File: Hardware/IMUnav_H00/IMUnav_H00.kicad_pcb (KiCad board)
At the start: 4 copper layers, 219 parts, among them J1 Conn_01x03_Pin, J2 Conn_01x03_Pin, J3 Conn_01x03_Pin, J4 Conn_01x03_Pin, J5 Conn_01x03_Pin, J6 Conn_01x03_Pin, J7 918-418K2023S40001, J8 Conn_Coaxial, J9 Micro_SD_Card_Det_Hirose_DM3AT, Q1 S8050, Q2 S8050, SW1 MT-102, SW2 SW_SPST, SW3 SW_SPST, SW4 SW_SPST, SW5 SW_SPST, U1 STM32F446VETx, U10 ESP32-C3-MINI-1, U11 MPU-6050, U12 LSM303C, U13 ADIS16505-2BMLZ, U14 ADIS16505-x/PCBZ, U15 XC6206P332MR, U16 NEO-M8U, U17 XT25F256BWSIGT, U18 OLED_I2C, U2 TVS0500DRV, U3 74LVC2G02, U4 BQ24075RGT, U5 USBLC6-2P6, U6 HT7533-1, U7 TPS62823DLC, U8 USB2514B-AEZC-TR, U9 CH340G, X1 SX5M24.000M20F30TNN, X2 SX5M24.000M20F30TNN

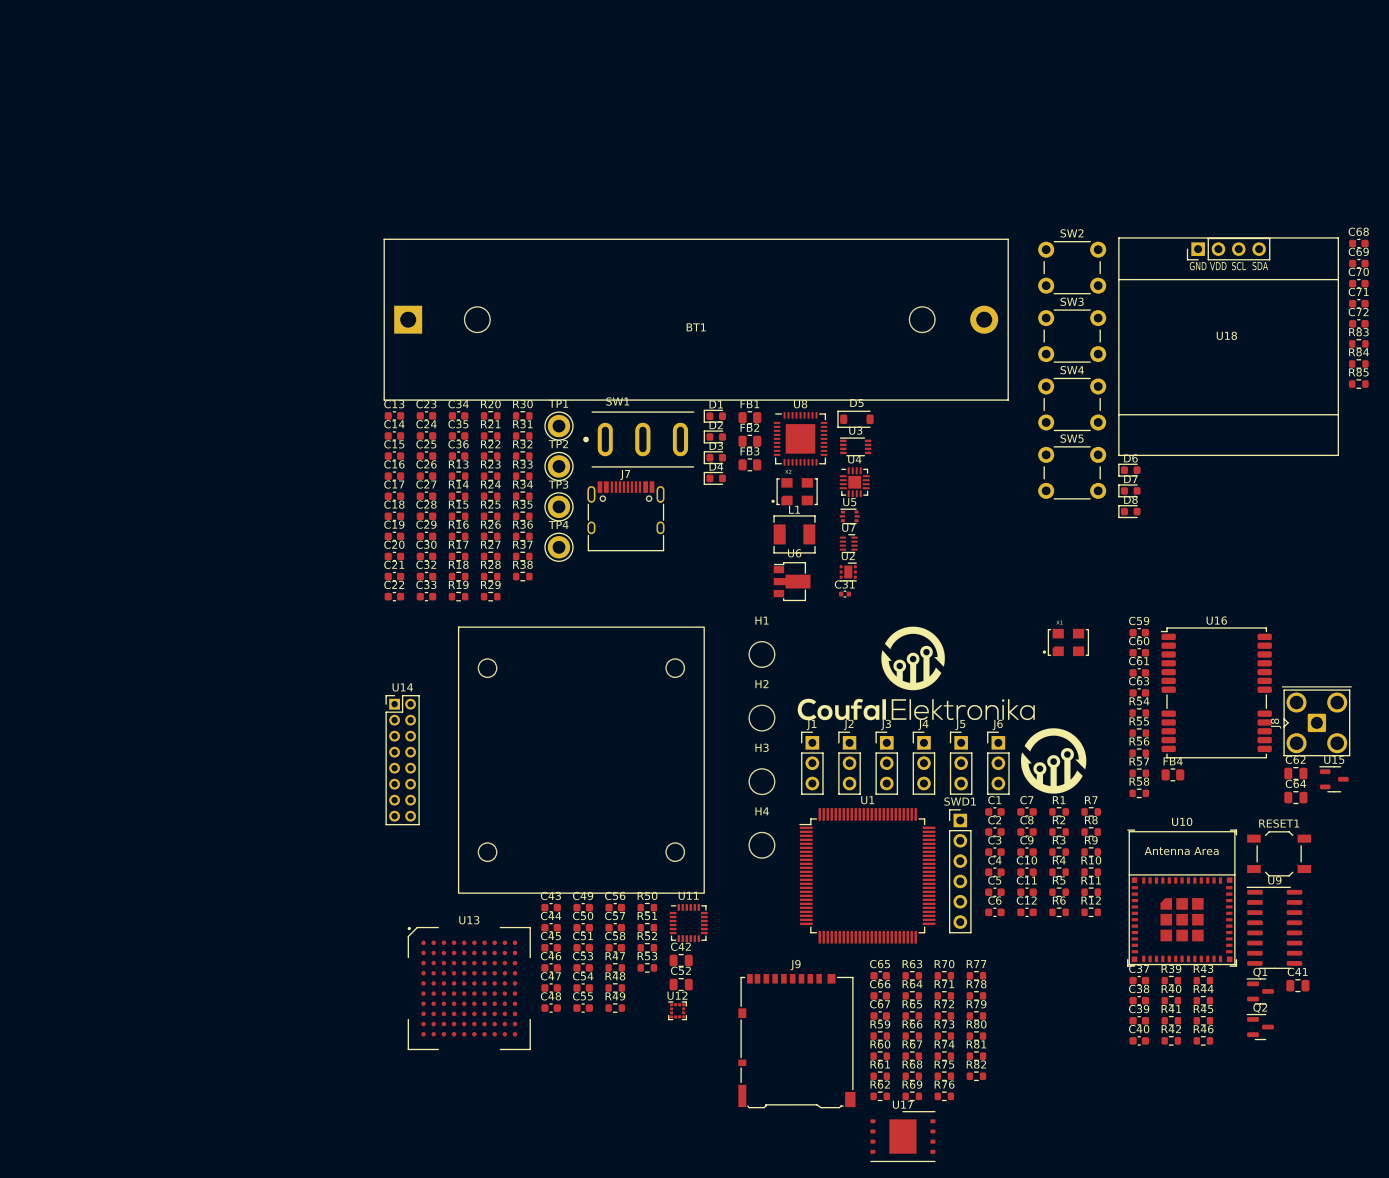
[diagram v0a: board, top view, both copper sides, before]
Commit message: Created PCB, configured stackup and DRC
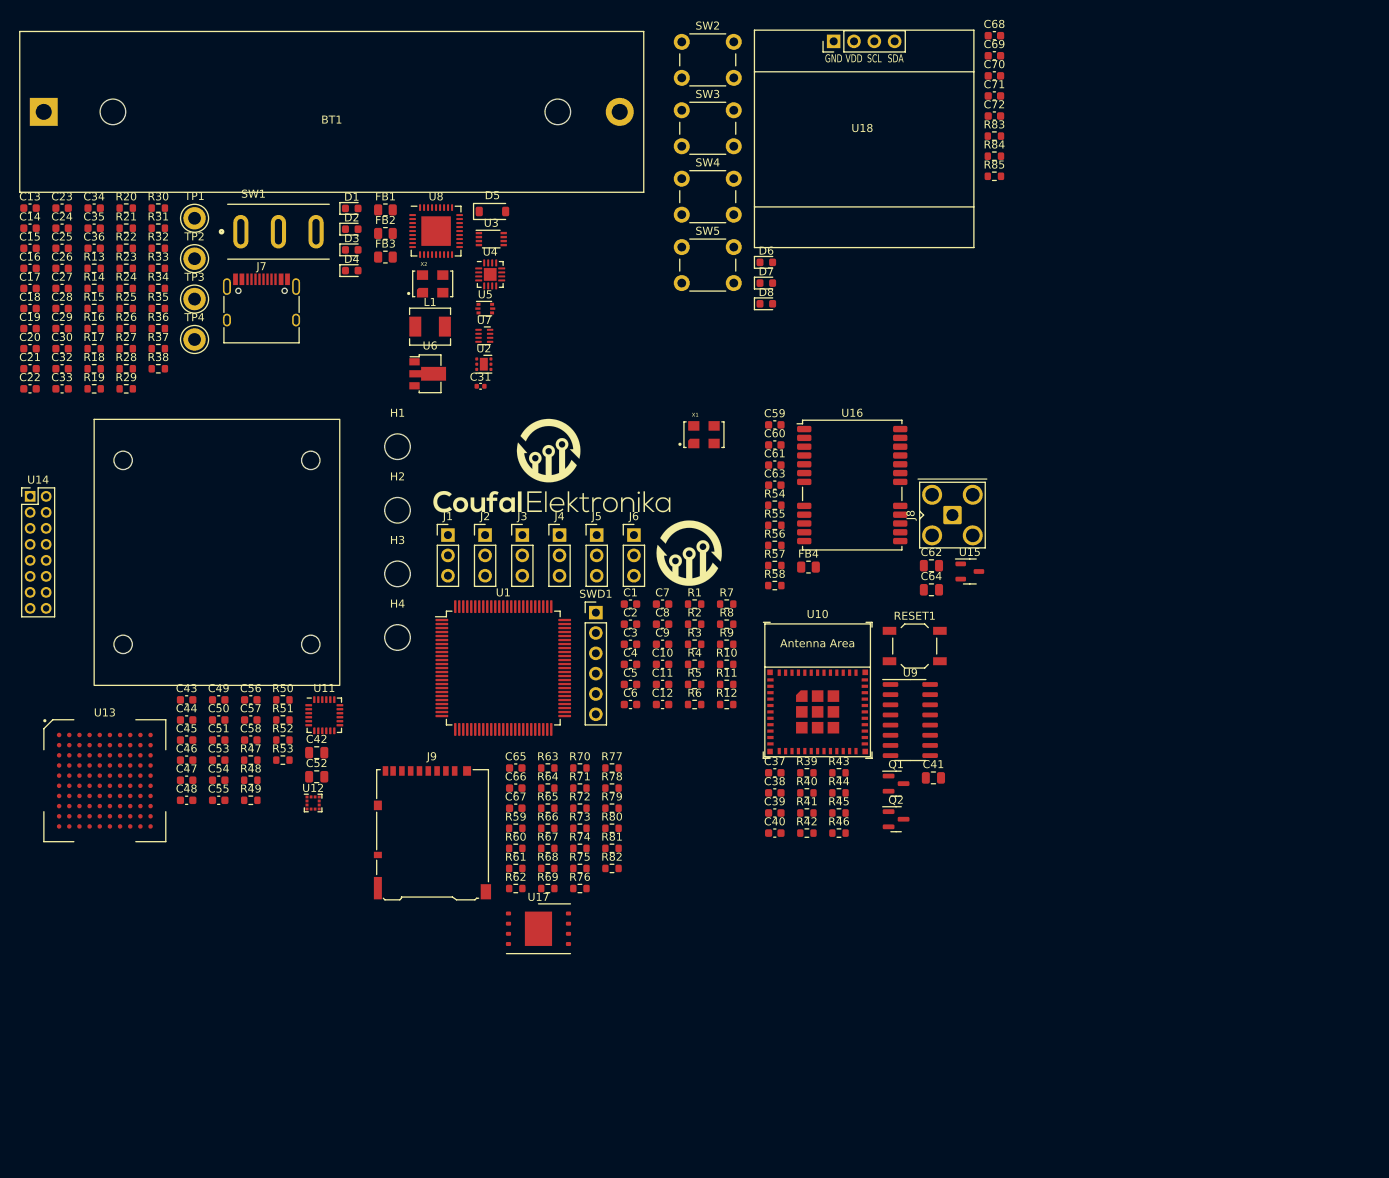
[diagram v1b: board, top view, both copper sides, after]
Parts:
- moved C44 52.4 mm to (21.1, 86.3)
- moved C47 52.4 mm to (21.1, 93.8)
- moved C67 52.4 mm to (62.2, 97.3)
- moved H4 52.4 mm to (47.4, 76.0)
- moved J1 52.4 mm to (53.7, 63.2)
- moved J2 52.4 mm to (58.4, 63.2)
- moved R51 52.4 mm to (33.1, 86.3)
- moved R60 52.4 mm to (62.2, 102.3)
- moved R62 52.4 mm to (62.2, 107.4)
- moved U13 52.4 mm to (10.9, 93.9)
- moved U14 52.4 mm to (9.53, 65.3)
- moved C1 52.4 mm to (76.6, 71.8)
- moved C2 52.4 mm to (76.6, 74.3)
- moved C3 52.4 mm to (76.6, 76.8)
- moved C4 52.4 mm to (76.6, 79.3)
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
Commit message: PCB layout - BGA fanout, GPS and USB hub
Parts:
- removed C54, C56, C58: 100n, Capacitor_SMD:C_0603_1608Metric
- C49: value 100n -> 220n
- J8: value Conn_Coaxial -> SMA6252A2-3GT50G-50
- U12: value LSM303C -> LSM303AGR
- moved BT1 111.5 mm to (-57.9, 103.5), turned to 90 degrees
- moved H3 108.2 mm to (151.1, 37.1)
- moved G1 106.0 mm to (172.1, 67.3)
- moved R54 101.5 mm to (28.8, -17.9)
- moved U15 96.4 mm to (46.0, 4.83)
- moved J8 96.4 mm to (38.5, 4.46)
- moved G2 90.5 mm to (172.7, 48.3)
- moved C24 90.2 mm to (-72.0, -21.3)
- moved C31 90.2 mm to (-19.7, -1.54)
- moved C33 90.2 mm to (-72.0, -1.22)
- moved C35 90.2 mm to (-68.0, -21.3)
- moved D5 90.2 mm to (-18.2, -23.4)
- moved FB2 90.2 mm to (-31.6, -20.6)
- moved FB3 90.2 mm to (-31.6, -17.7)
- moved R13 90.2 mm to (-68.0, -16.3)
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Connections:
- net LSM_INTACCL renamed LSM_INT1ACCL
- net LSM_MAGDRDY renamed LSM_INT2ACCL
- net Net-(C22-Pad1) renamed /USB+Power/+3V3USB
- J9 pad 11: unconnected-(J9-SHIELD-Pad11) -> GND
- U13 pad A9: unconnected-(U13-NC-PadA10) -> unconnected-(U13-NC-PadA9)
- U13 pad B1: unconnected-(U13-NC-PadA10) -> unconnected-(U13-NC-PadB1)
- U13 pad B10: unconnected-(U13-NC-PadA10) -> unconnected-(U13-NC-PadB10)
- U13 pad B2: unconnected-(U13-NC-PadA10) -> unconnected-(U13-NC-PadB2)
- U13 pad B7: unconnected-(U13-NC-PadA10) -> unconnected-(U13-NC-PadB7)
- U13 pad B8: unconnected-(U13-NC-PadA10) -> unconnected-(U13-NC-PadB8)
- U13 pad B9: unconnected-(U13-NC-PadA10) -> unconnected-(U13-NC-PadB9)
- U13 pad C1: unconnected-(U13-NC-PadA10) -> unconnected-(U13-NC-PadC1)
- U13 pad C10: unconnected-(U13-NC-PadA10) -> unconnected-(U13-NC-PadC10)
- U13 pad C4: unconnected-(U13-NC-PadA10) -> unconnected-(U13-NC-PadC4)
- U13 pad C5: unconnected-(U13-NC-PadA10) -> unconnected-(U13-NC-PadC5)
- U13 pad C8: unconnected-(U13-NC-PadA10) -> unconnected-(U13-NC-PadC8)
- U13 pad C9: unconnected-(U13-NC-PadA10) -> unconnected-(U13-NC-PadC9)
- U13 pad D1: unconnected-(U13-NC-PadA10) -> unconnected-(U13-NC-PadD1)
- U13 pad D10: unconnected-(U13-NC-PadA10) -> unconnected-(U13-NC-PadD10)
- U13 pad D2: unconnected-(U13-NC-PadA10) -> unconnected-(U13-NC-PadD2)
- U13 pad D4: unconnected-(U13-NC-PadA10) -> unconnected-(U13-NC-PadD4)
- U13 pad D5: unconnected-(U13-NC-PadA10) -> unconnected-(U13-NC-PadD5)
- U13 pad D7: unconnected-(U13-NC-PadA10) -> unconnected-(U13-NC-PadD7)
- U13 pad D8: unconnected-(U13-NC-PadA10) -> unconnected-(U13-NC-PadD8)
- U13 pad D9: unconnected-(U13-NC-PadA10) -> unconnected-(U13-NC-PadD9)
- U13 pad E1: unconnected-(U13-NC-PadA10) -> unconnected-(U13-NC-PadE1)
- U13 pad E10: unconnected-(U13-NC-PadA10) -> unconnected-(U13-NC-PadE10)
- U13 pad E4: unconnected-(U13-NC-PadA10) -> unconnected-(U13-NC-PadE4)
- U13 pad E5: unconnected-(U13-NC-PadA10) -> unconnected-(U13-NC-PadE5)
- U13 pad E8: unconnected-(U13-NC-PadA10) -> unconnected-(U13-NC-PadE8)
- U13 pad E9: unconnected-(U13-NC-PadA10) -> unconnected-(U13-NC-PadE9)
- U13 pad F10: unconnected-(U13-NC-PadA10) -> unconnected-(U13-NC-PadF10)
- U13 pad F2: unconnected-(U13-NC-PadA10) -> unconnected-(U13-NC-PadF2)
- U13 pad F4: unconnected-(U13-NC-PadA10) -> unconnected-(U13-NC-PadF4)
- U13 pad F7: unconnected-(U13-NC-PadA10) -> unconnected-(U13-NC-PadF7)
- U13 pad F9: unconnected-(U13-NC-PadA10) -> unconnected-(U13-NC-PadF9)
- U13 pad G10: unconnected-(U13-NC-PadA10) -> unconnected-(U13-NC-PadG10)
- U13 pad G4: unconnected-(U13-NC-PadA10) -> unconnected-(U13-NC-PadG4)
- U13 pad G5: unconnected-(U13-NC-PadA10) -> unconnected-(U13-NC-PadG5)
- U13 pad G8: unconnected-(U13-NC-PadA10) -> unconnected-(U13-NC-PadG8)
- U13 pad G9: unconnected-(U13-NC-PadA10) -> unconnected-(U13-NC-PadG9)
- U13 pad H10: unconnected-(U13-NC-PadA10) -> unconnected-(U13-NC-PadH10)
- U13 pad H2: unconnected-(U13-NC-PadA10) -> unconnected-(U13-NC-PadH2)
- U13 pad H4: unconnected-(U13-NC-PadA10) -> unconnected-(U13-NC-PadH4)
- U13 pad H5: unconnected-(U13-NC-PadA10) -> unconnected-(U13-NC-PadH5)
- U13 pad H7: unconnected-(U13-NC-PadA10) -> unconnected-(U13-NC-PadH7)
- U13 pad H9: unconnected-(U13-NC-PadA10) -> unconnected-(U13-NC-PadH9)
- U13 pad J1: unconnected-(U13-NC-PadA10) -> unconnected-(U13-NC-PadJ1)
- U13 pad J10: unconnected-(U13-NC-PadA10) -> unconnected-(U13-NC-PadJ10)
- U13 pad J8: unconnected-(U13-NC-PadA10) -> unconnected-(U13-NC-PadJ8)
- U13 pad J9: unconnected-(U13-NC-PadA10) -> unconnected-(U13-NC-PadJ9)
- U13 pad K10: unconnected-(U13-NC-PadA10) -> unconnected-(U13-NC-PadK10)
- U13 pad K2: unconnected-(U13-NC-PadA10) -> unconnected-(U13-NC-PadK2)
- U13 pad K4: unconnected-(U13-NC-PadA10) -> unconnected-(U13-NC-PadK4)
- U13 pad K5: unconnected-(U13-NC-PadA10) -> unconnected-(U13-NC-PadK5)
- U13 pad K7: unconnected-(U13-NC-PadA10) -> unconnected-(U13-NC-PadK7)
- U13 pad K9: unconnected-(U13-NC-PadA10) -> unconnected-(U13-NC-PadK9)
- U14 pad 16: unconnected-(U14-NC-Pad15) -> unconnected-(U14-NC-Pad16)
- U14 pad 5: unconnected-(U14-NC-Pad15) -> unconnected-(U14-NC-Pad5)
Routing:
- net GND: track 0.00 -> 59.3 mm, vias 0 -> 62
- net /USB+Power/+3V3USB: track 0.00 -> 27.6 mm, vias 0 -> 4
- net +3V3: track 0.00 -> 26.1 mm, vias 0 -> 11
- net +5V: track 0.00 -> 21.7 mm, vias 0 -> 6
- net Net-(U15-VO): track 0.00 -> 13.8 mm
- net Net-(U8-XTALIN/CLKIN): track 0.00 -> 13.5 mm
- net /USB+Power/D+: track 0.00 -> 12.7 mm
- net /USB+Power/D-: track 0.00 -> 12.3 mm
- net Net-(J8-In): track 0.00 -> 10.1 mm
- net /GPS/GPS_D-: track 0.00 -> 8.03 mm
- net Net-(U16-USB_DP): track 0.00 -> 7.66 mm
- net /GPS/GPS_D+: track 0.00 -> 7.63 mm
- net /USB+Power/USB3_D-: track 0.00 -> 7.05 mm
- net /USB+Power/USB3_D+: track 0.00 -> 6.65 mm
- net /ESP32/ESP_D-: track 0.00 -> 6.16 mm
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- added copper zone on In2.Cu, net +3V3
- added copper zone on In2.Cu, net +5V
- added copper zone on F.Cu, net GND
- added copper zone on In1.Cu, net GND
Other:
- board outline added: 100 x 100 mm
- board text added: "USB"

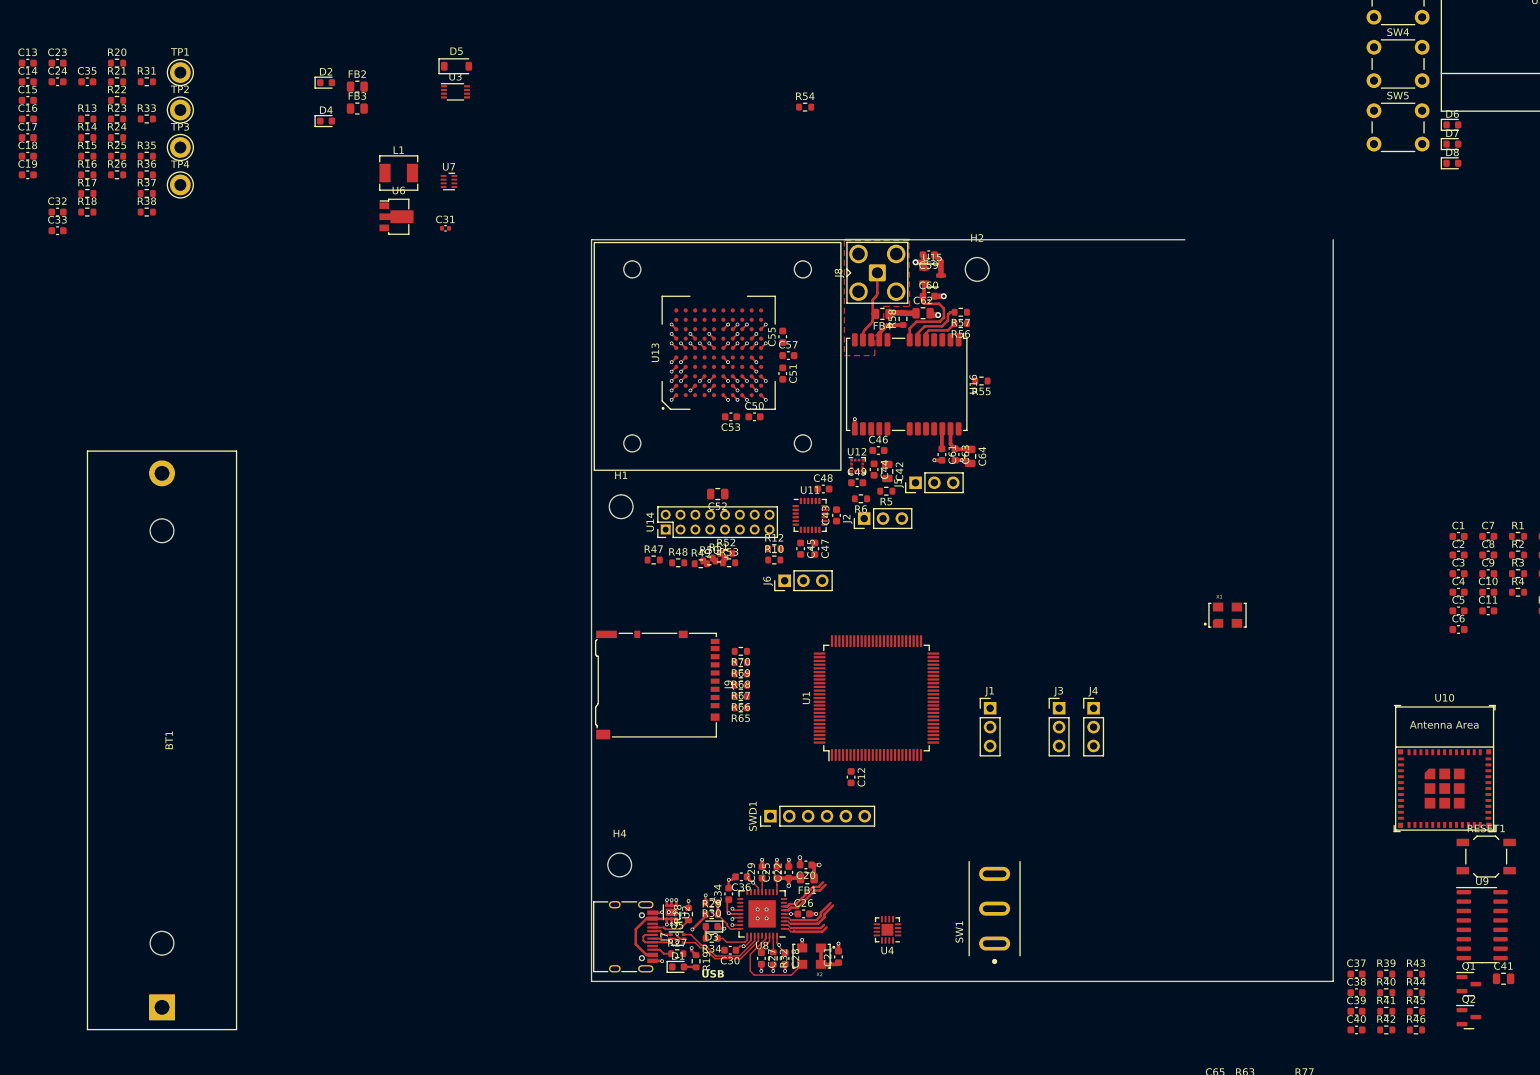
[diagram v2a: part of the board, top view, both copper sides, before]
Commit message: USB charger layout
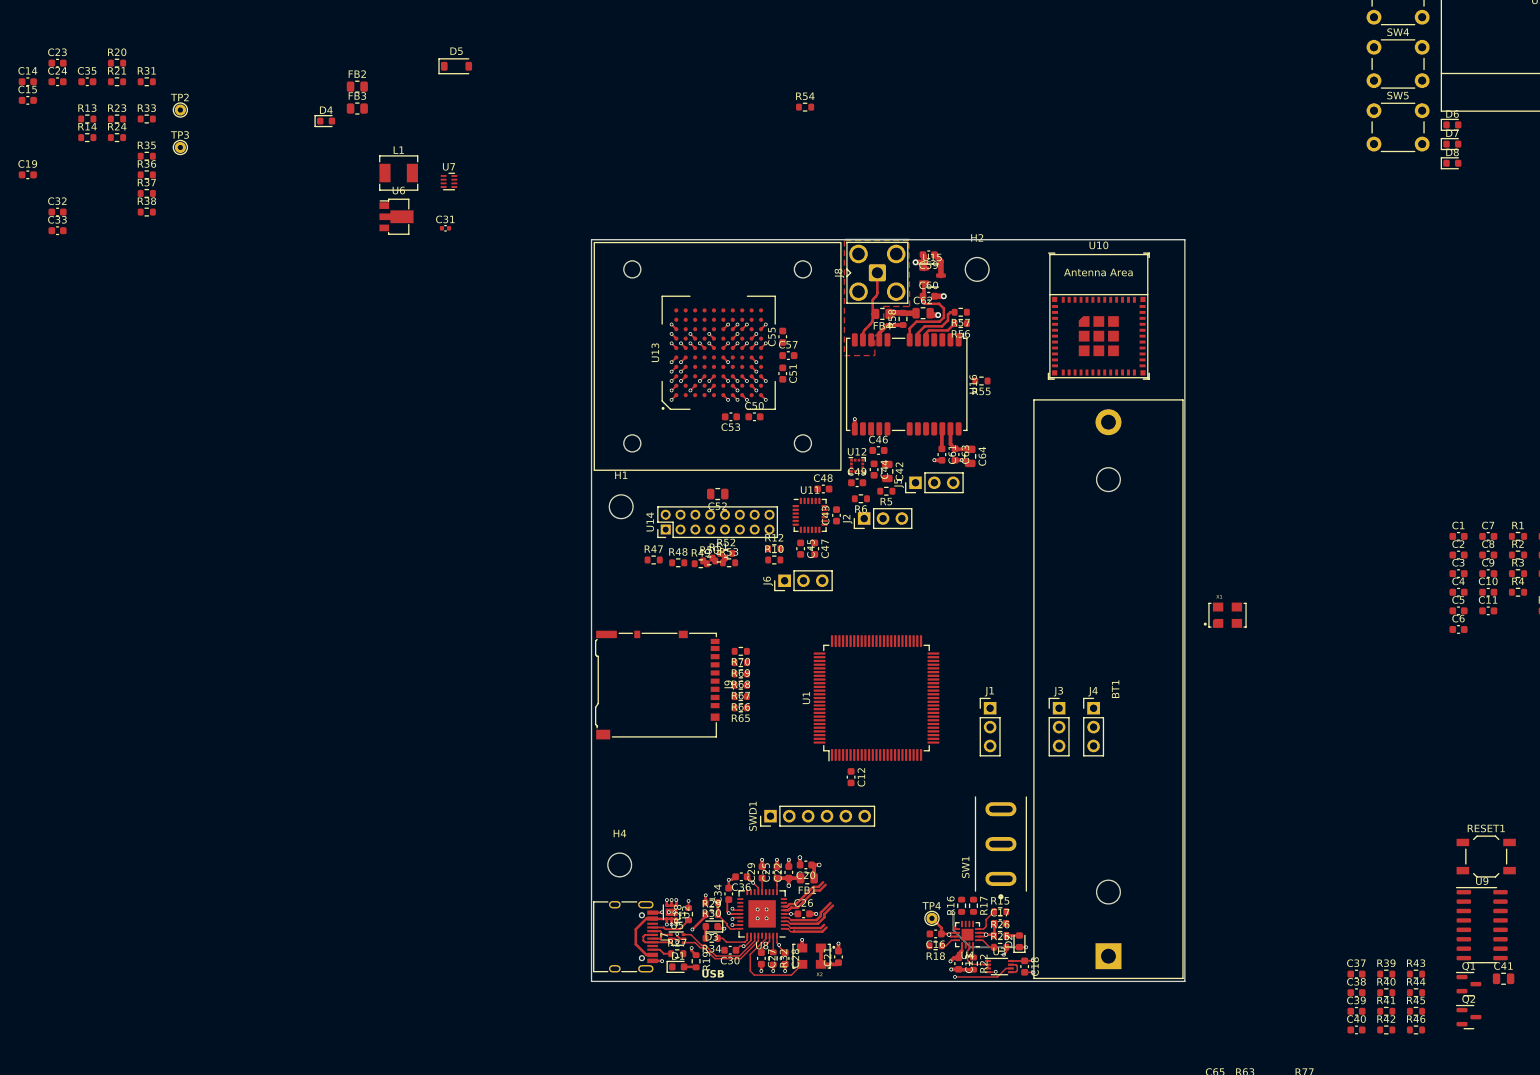
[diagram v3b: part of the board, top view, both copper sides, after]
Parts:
- removed TP1: TestPoint, TestPoint:TestPoint_Keystone_5005-5009_Compact
- TP2, TP3, TP4: footprint TestPoint:TestPoint_Keystone_5005-5009_Compact -> TestPoint:TestPoint_THTPad_D1.5mm_Drill0.7mm
- moved C13 174.6 mm to (49.5, 97.6), turned to -90 degrees
- moved C18 173.2 mm to (58.4, 98.0), turned to -90 degrees
- moved C17 168.6 mm to (55.1, 92.2)
- moved C16 164.5 mm to (46.4, 93.6), turned to 180 degrees
- moved R22 164.0 mm to (51.5, 97.6), turned to -90 degrees
- moved R25 159.9 mm to (55.1, 95.4)
- moved R15 159.8 mm to (55.1, 90.6)
- moved R26 157.1 mm to (55.1, 93.8)
- moved R16 153.7 mm to (49.9, 89.8), turned to 90 degrees
- moved R17 153.3 mm to (51.5, 89.8), turned to -90 degrees
- moved R18 151.2 mm to (46.4, 95.2), turned to 180 degrees
- moved D2 148.8 mm to (57.7, 94.6), turned to 90 degrees
- moved TP4 141.6 mm to (45.9, 91.5)
- moved U3 138.9 mm to (55.0, 98.0)
- moved BT1 127.8 mm to (69.7, 96.6)
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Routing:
- net Net-(BT1-+): track 0.00 -> 29.2 mm, vias 0 -> 2
- net Net-(D2-K): track 0.00 -> 16.3 mm, vias 0 -> 2
- net +5V: track 21.7 -> 32.9 mm, vias 6 -> 8
- net GND: track 59.3 -> 65.7 mm, vias 62 -> 66
- net Net-(SW1-B): track 0.00 -> 6.03 mm, vias 0 -> 1
- net Net-(U4-SYSOFF): track 0.00 -> 5.62 mm
- net Net-(U4-~{CE}): track 0.00 -> 3.65 mm
- net Net-(U4-TS): track 0.00 -> 2.53 mm
- net Net-(U3-Pad5): track 0.00 -> 2.47 mm
- net Net-(U4-ILIM): track 0.00 -> 2.35 mm
- net Net-(D2-A): track 0.00 -> 1.78 mm
- net Net-(U4-ISET): track 0.00 -> 1.66 mm
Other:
- board size 100 x 100 mm -> 80 x 100 mm
